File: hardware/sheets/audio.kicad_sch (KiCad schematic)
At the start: 17 parts, among them J1 PicoGUS_LineIn, J2 LineOut_TRS, U1 MCP6002

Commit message: JLCPCB sourcing pass: verify pinouts, LCSC part numbers, SMD build
Custom-symbol verification (open-questions Q5 resolved):
- MAX3241 symbol was wrong on nearly every pin and used MAX3243-style
  control names; regenerated to the real SSOP-28 pinout (SHDN#/EN#/
  R1OUTB/R2OUTB) and com_port rewired -- EN# must be GROUNDED (the old
  ~FORCEON-high would have disabled the receivers on real silicon)
- DS12C887 symbol wrong on 4 pins (DS=17, RESET#=18, IRQ#=19, SQW=23)

Sourcing (every part checked against the JLC DB; ~45 line items):
- New tools/parts.py maps (lib_id, value) -> LCSC; build.py applies it as
  an 'LCSC Part Num' property on every component (384 across the project)
- Sheets stay generic; stock-forced substitutions bound in the map:
  '374->'574 (parallel rewired), '163->'161, '157->HC157 (+HCT-buffered
  3.3V selects, I0/I1 swapped), '02->HC02, TCM809->MCP809, 2N3904->MMBT3904
- bus_mcu address counters moved to the 3.3V domain (HC161 on 3V3_BUS,
  loaded from MCU-side MD0-7; HCT244s read the 3.3V outputs at TTL Vih)
- 14.318 XOs are 3.3V-only parts: powered from 3V3, squared up via spare
  HCT gates (cpu_core U13, card_isatest U19)
- COM baud reference is now a 1.8432MHz crystal on the 16C550's XIN/XOUT
  (3.3V-only oscillators vs a 5V-only soft card)
- Supervisor QSPI header replaced with a real W25Q128JVSIQ
- Socket policy (fab installs sockets): V20 DIP-40, SRAM DIP-32 (no 5V
  512Kx8 SRAM at JLC at all), DS12C887 DIP-24, female headers for modules

Docs: CLAUDE.md fabrication-constraints section (SMD, 100x100mm, generic-
symbols rule, voltage-domain rule); README + hardware/README fab notes;
notes/jlcpcb-sourcing.md (decisions, thin-stock flags, not-at-JLC list);
stale questions-sidecar.md collapsed to its supersession record.

Rebuilt motherboard + cards: structural ERC 0, byte-identical rebuilds.

Co-Authored-By: Claude Fable 5 <noreply@anthropic.com>
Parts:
- C1, C7: LCSC Part Num (none) -> C15850
- C2: LCSC Part Num (none) -> C57112
- C3, C4, C5: LCSC Part Num (none) -> C15849
- C6: LCSC Part Num (none) -> C14663
- J1, J2: LCSC Part Num (none) -> C2337
- R1, R10, R2, R4, R5, R6: LCSC Part Num (none) -> C25804
- R3: LCSC Part Num (none) -> C21190
- U1: LCSC Part Num (none) -> C7377
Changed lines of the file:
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@@
+			)
+		)
+		(property "LCSC Part Num" "C25804"
+			(at 50.8 76.2 0)
+			(effects
+				(font
+					(size 1.27 1.27)
+				)
+				(hide yes)
 			)
 		)
@@
 			)
 		)
+		(property "LCSC Part Num" "C25804"
+			(at 50.8 109.22 0)
+			(effects
+				(font
+					(size 1.27 1.27)
+				)
+				(hide yes)
+			)
+		)
 		(pin "1"
 		)
@@
 			)
 		)
+		(property "LCSC Part Num" "C15850"
+			(at 76.2 109.22 0)
+			(effects
+				(font
+					(size 1.27 1.27)
+				)
+				(hide yes)
+			)
+		)
 		(pin "1"
 		)
@@
 			)
 		)
+		(property "LCSC Part Num" "C21190"
+			(at 50.8 165.1 0)
+			(effects
+				(font
+					(size 1.27 1.27)
+				)
+				(hide yes)
+			)
+		)
 		(pin "1"
 		)
@@
 			)
 		)
+		(property "LCSC Part Num" "C57112"
+			(at 76.2 198.12 0)
+			(effects
+				(font
+					(size 1.27 1.27)
+				)
+				(hide yes)
+			)
+		)
 		(pin "1"
 		)
@@
 			)
 		)
+		(property "LCSC Part Num" "C15849"
+			(at 101.6 165.1 0)
+			(effects
+				(font
+					(size 1.27 1.27)
+				)
+				(hide yes)
+			)
+		)
 		(pin "1"
 		)
@@
 			)
 		)
+		(property "LCSC Part Num" "C2337"
+			(at 50.8 228.6 0)
+			(effects
+				(font
+					(size 1.27 1.27)
+				)
+				(hide yes)
+			)
+		)
 		(pin "1"
 		)
@@
 			)
 		)
+		(property "LCSC Part Num" "C15849"
+			(at 101.6 215.9 0)
+			(effects
+				(font
+					(size 1.27 1.27)
+				)
+				(hide yes)
+			)
+		)
 		(pin "1"
 		)
@@
 			)
 		)
+		(property "LCSC Part Num" "C15849"
+			(at 101.6 241.3 0)
+			(effects
+				(font
+					(size 1.27 1.27)
+				)
+				(hide yes)
+			)
+		)
 		(pin "1"
 		)
@@
 			)
 		)
+		(property "LCSC Part Num" "C7377"
+			(at 177.8 152.4 0)
+			(effects
+				(font
+					(size 1.27 1.27)
+				)
+				(hide yes)
+			)
+		)
 		(pin "3"
 		)
@@
 			)
 		)
+		(property "LCSC Part Num" "C14663"
+			(at 203.2 101.6 0)
+			(effects
+				(font
+					(size 1.27 1.27)
+				)
+				(hide yes)
+			)
+		)
 		(pin "1"
 		)
@@
 			)
 		)
+		(property "LCSC Part Num" "C25804"
+			(at 127 127 0)
+			(effects
+				(font
+					(size 1.27 1.27)
+				)
+				(hide yes)
+			)
+		)
 		(pin "1"
 		)
@@
 			)
 		)
+		(property "LCSC Part Num" "C25804"
+			(at 152.4 127 0)
+			(effects
+				(font
+					(size 1.27 1.27)
+				)
+				(hide yes)
+			)
+		)
 		(pin "1"
 		)
@@
 			)
 		)
+		(property "LCSC Part Num" "C25804"
+			(at 152.4 177.8 0)
+			(effects
+				(font
+					(size 1.27 1.27)
+				)
+				(hide yes)
+			)
+		)
 		(pin "1"
 		)
@@
 			)
 		)
+		(property "LCSC Part Num" "C25804"
+			(at 203.2 127 0)
+			(effects
+				(font
+					(size 1.27 1.27)
+				)
+				(hide yes)
+			)
+		)
 		(pin "1"
 		)
@@
 			)
 		)
+		(property "LCSC Part Num" "C15850"
+			(at 228.6 127 0)
+			(effects
+				(font
+					(size 1.27 1.27)
+				)
+				(hide yes)
+			)
+		)
 		(pin "1"
 		)
@@
 			(at 266.7 152.4 0)
 			(effects
+				(font
+					(size 1.27 1.27)
+				)
+				(hide yes)
+			)
+		)
+		(property "LCSC Part Num" "C2337"
+			(at 266.7 152.4 0)
+			(effects

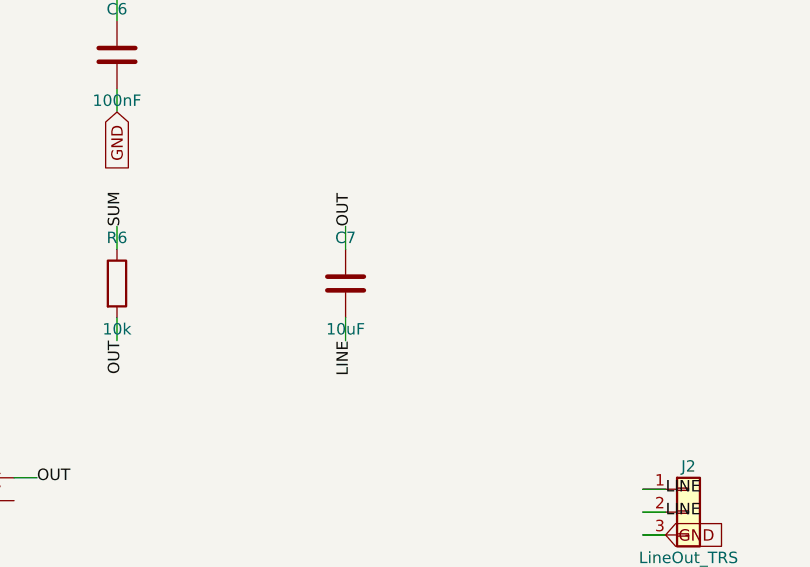
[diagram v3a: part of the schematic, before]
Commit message: Design review 2026-07-11: rail protection, decoupling, wiring fixes
Protection:
- Sidecar +5V now feeds through a 2A polyfuse into +5V_ISA with an
  SMBJ5.0A clamp + 22uF bulk (a faulted ISA card trips its own fuse
  instead of dropping the board; back-fed voltage is clamped).
- USB-C VBUS enters through a 3A polyfuse with an SMBJ5.0A on +5V
  (backstop for the CFG1 9-20V failure mode). CH224K gains a 1uF VDD
  cap; its PG routes to Supervisor GPIO16 as PD_PG. Buck output
  doubled to 2x22uF, 10uF at VIN, extra rail bulk.
- Supervisor USB-A host port: 27R series termination (RP2040
  requirement), USBLC6-2SC6 ESD array, 100uF VBUS bulk.
- Video: HDMI +5V fused (500mA), HPD sensed on GPIO41, 100R series on
  VGA sync. TMDS ESD array deferred to layout (no symbol).
- card_isatest: V5RAW bulk, Q1 gate soft-start cap, TVS on DUT rail.

Wiring fixes:
- SPKR had no driver anywhere (netlist: 1 node). Bus MCU GPIO22
  reassigned from the diagnostics-only bus-CLK sense to SPKR; bus_mcu
  drops CLK from its interface. Doc 5.2 updated.
- bus_mcu C8 decoupled +3V3, a rail that sheet never uses -> 3V3_BUS.
- Storage IRQ5 was push-pull (permanently driven when idle) -> 2N7002
  + gated '125 tri-state, same convention as the LPT IRQ7 stage.
- MAX3241 pump caps resized to the 5V datasheet values (47nF/330nF).
- LPT DB25 status inputs get 4.7k pull-ups (floated with no printer).
- Audio line-out gets a 100R series isolator before the jack.

Best practices:
- Decoupling to ~1x100nF per IC on every sheet + bulk per board
  (cpu_core 7->16 incl. the naked 3.3V oscillator, storage 4->11,
  parallel 6->13, rtc/com/video/bus_mcu/card_isatest similar).
- All floating spare CMOS inputs tied ('00/'74/'157/'02/'04/'125
  sections across cpu_core, bus_mcu, rtc, storage, card_isatest).

Sourcing: new parts mapped in parts.py with JLC-verified LCSC numbers;
Power_Protection lib registered in the tools; TPS563200 stock alert
(4 pcs left at JLC) flagged in parts.py + jlcpcb-sourcing.md. All
decisi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
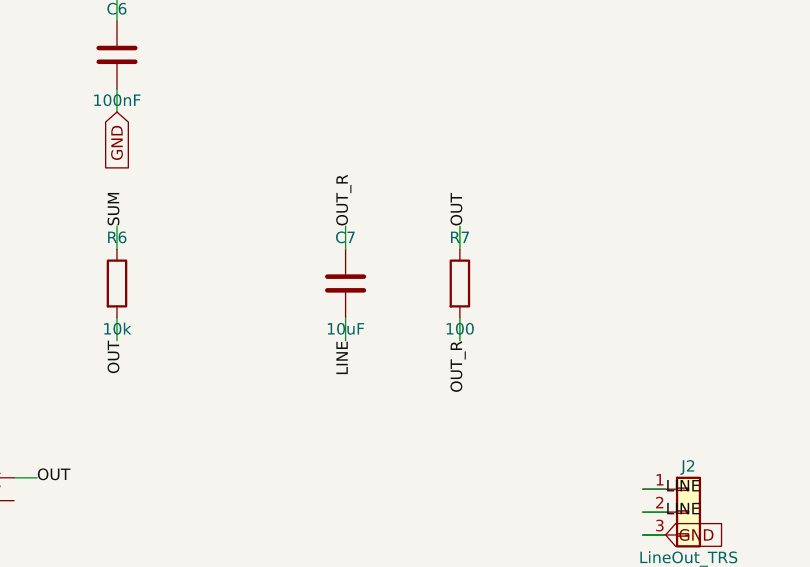
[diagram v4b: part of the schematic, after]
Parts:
- added J2: LineOut_TRS, symbol Connector_Generic:Conn_01x03
- C7: renamed from J2; value LineOut_TRS -> 10uF; symbol Connector_Generic:Conn_01x03 -> Device:C; LCSC Part Num C2337 -> C15850
- R7: renamed from C7; value 10uF -> 100; symbol Device:C -> Device:R; LCSC Part Num C15850 -> C22775
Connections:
- net GND: now also J2.3 (Pin_3); no longer C7.3 (Pin_3)
- net LINE: now also J2.1 (Pin_1), J2.2 (Pin_2); no longer C7.1 (Pin_1), R7.2
- new net OUT_R: C7.1, R7.2
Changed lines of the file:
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@@
+	(wire
+		(pts
+			(xy 241.3 123.19)
+			(xy 241.3 120.65)
+		)
+		(stroke
+			(width 0)
+			(type default)
+		)
+	)
+	(label "OUT"
+		(at 241.3 120.65 90)
+		(effects
+			(font
+				(size 1.27 1.27)
+			)
+		)
+	)
+	(wire
+		(pts
+			(xy 241.3 130.81)
+			(xy 241.3 133.35)
+		)
+		(stroke
+			(width 0)
+			(type default)
+		)
+	)
+	(label "OUT_R"
+		(at 241.3 133.35 270)
+		(effects
+			(font
+				(size 1.27 1.27)
+			)
+		)
+	)
 	(wire
 		(pts
@@
 		)
 	)
-	(label "OUT"
+	(label "OUT_R"
 		(at 228.6 120.65 90)
 		(effects
@@
 		(instances
 			(project "mini-xt"
-				(path "/26736c46-8b40-5460-874f-03596d17270c/130b8a0a-419b-58f7-be98-d1ab6f413e73"
+				(path "/26736c46-8b40-5460-874f-03596d17270c/eddc1827-22a2-582d-9105-2ac11ccaf77c"
 					(reference "R1101")
 					(unit 1)
@@
 		(instances
 			(project "mini-xt"
-				(path "/26736c46-8b40-5460-874f-03596d17270c/130b8a0a-419b-58f7-be98-d1ab6f413e73"
+				(path "/26736c46-8b40-5460-874f-03596d17270c/eddc1827-22a2-582d-9105-2ac11ccaf77c"
 					(reference "R1102")
 					(unit 1)
@@
 		(instances
 			(project "mini-xt"
-				(path "/26736c46-8b40-5460-874f-03596d17270c/130b8a0a-419b-58f7-be98-d1ab6f413e73"
+				(path "/26736c46-8b40-5460-874f-03596d17270c/eddc1827-22a2-582d-9105-2ac11ccaf77c"
 					(reference "C1101")
 					(unit 1)
@@
 		(instances
 			(project "mini-xt"
-				(path "/26736c46-8b40-5460-874f-03596d17270c/130b8a0a-419b-58f7-be98-d1ab6f413e73"
+				(path "/26736c46-8b40-5460-874f-03596d17270c/eddc1827-22a2-582d-9105-2ac11ccaf77c"
 					(reference "R1103")
 					(unit 1)
@@
 		(instances
 			(project "mini-xt"
-				(path "/26736c46-8b40-5460-874f-03596d17270c/130b8a0a-419b-58f7-be98-d1ab6f413e73"
+				(path "/26736c46-8b40-5460-874f-03596d17270c/eddc1827-22a2-582d-9105-2ac11ccaf77c"
 					(reference "C1102")
 					(unit 1)
@@
 		(instances
 			(project "mini-xt"
-				(path "/26736c46-8b40-5460-874f-03596d17270c/130b8a0a-419b-58f7-be98-d1ab6f413e73"
+				(path "/26736c46-8b40-5460-874f-03596d17270c/eddc1827-22a2-582d-9105-2ac11ccaf77c"
 					(reference "C1103")
 					(unit 1)
@@
 		(instances
 			(project "mini-xt"
-				(path "/26736c46-8b40-5460-874f-03596d17270c/130b8a0a-419b-58f7-be98-d1ab6f413e73"
+				(path "/26736c46-8b40-5460-874f-03596d17270c/eddc1827-22a2-582d-9105-2ac11ccaf77c"
 					(reference "J1101")
 					(unit 1)
@@
 		(instances
 			(project "mini-xt"
-				(path "/26736c46-8b40-5460-874f-03596d17270c/130b8a0a-419b-58f7-be98-d1ab6f413e73"
+				(path "/26736c46-8b40-5460-874f-03596d17270c/eddc1827-22a2-582d-9105-2ac11ccaf77c"
 					(reference "C1104")
 					(unit 1)
@@
 		(instances
 			(project "mini-xt"
-				(path "/26736c46-8b40-5460-874f-03596d17270c/130b8a0a-419b-58f7-be98-d1ab6f413e73"
+				(path "/26736c46-8b40-5460-874f-03596d17270c/eddc1827-22a2-582d-9105-2ac11ccaf77c"
 					(reference "C1105")
 					(unit 1)
@@
 		(instances
 			(project "mini-xt"
-				(path "/26736c46-8b40-5460-874f-03596d17270c/130b8a0a-419b-58f7-be98-d1ab6f413e73"
+				(path "/26736c46-8b40-5460-874f-03596d17270c/eddc1827-22a2-582d-9105-2ac11ccaf77c"
 					(reference "U1101")
 					(unit 1)
@@
 		(instances
 			(project "mini-xt"
-				(path "/26736c46-8b40-5460-874f-03596d17270c/130b8a0a-419b-58f7-be98-d1ab6f413e73"
+				(path "/26736c46-8b40-5460-874f-03596d17270c/eddc1827-22a2-582d-9105-2ac11ccaf77c"
 					(reference "C1106")
 					(unit 1)
@@
 		(instances
 			(project "mini-xt"
-				(path "/26736c46-8b40-5460-874f-03596d17270c/130b8a0a-419b-58f7-be98-d1ab6f413e73"
+				(path "/26736c46-8b40-5460-874f-03596d17270c/eddc1827-22a2-582d-9105-2ac11ccaf77c"
 					(reference "R1104")
 					(unit 1)
@@
 		(instances
 			(project "mini-xt"
-				(path "/26736c46-8b40-5460-874f-03596d17270c/130b8a0a-419b-58f7-be98-d1ab6f413e73"
+				(path "/26736c46-8b40-5460-874f-03596d17270c/eddc1827-22a2-582d-9105-2ac11ccaf77c"
 					(reference "R1105")
 					(unit 1)
@@
 		(instances
 			(project "mini-xt"
-				(path "/26736c46-8b40-5460-874f-03596d17270c/130b8a0a-419b-58f7-be98-d1ab6f413e73"
+				(path "/26736c46-8b40-5460-874f-03596d17270c/eddc1827-22a2-582d-9105-2ac11ccaf77c"
 					(reference "R1110")
 					(unit 1)
@@
 		(instances
 			(project "mini-xt"
-				(path "/26736c46-8b40-5460-874f-03596d17270c/130b8a0a-419b-58f7-be98-d1ab6f413e73"
+				(path "/26736c46-8b40-5460-874f-03596d17270c/eddc1827-22a2-582d-9105-2ac11ccaf77c"
 					(reference "R1106")
+					(unit 1)
+				)
+			)
+		)
+	)
+	(symbol
+		(lib_id "Device:R")
+		(at 241.3 127 0)
+		(unit 1)
+		(exclude_from_sim no)
+		(in_bom yes)
+		(on_board yes)
+		(dnp no)
+		(fields_autoplaced yes)
+		(property "Reference" "R7"
+			(at 241.3 121.92 0)
+			(effects
+				(font
+					(size 1.27 1.27)
+				)
+			)
+		)
+		(property "Value" "100"
+			(at 241.3 132.08 0)
+			(effects
+				(font
+					(size 1.27 1.27)
+				)
+			)
+		)
+		(property "Footprint" ""
+			(at 241.3 127 0)
+			(effects
+				(font
+					(size 1.27 1.27)
+				)
+				(hide yes)
+			)
+		)
+		(property "LCSC Part Num" "C22775"
+			(at 241.3 127 0)
+			(effects
+				(font
+					(size 1.27 1.27)
+				)
+				(hide yes)
+			)
+		)
+		(pin "1"
+		)
+		(pin "2"
+		)
+		(instances
+			(project "mini-xt"
+				(path "/26736c46-8b40-5460-874f-03596d17270c/eddc1827-22a2-582d-9105-2ac11ccaf77c"
+					(reference "R1107")
 					(unit 1)
 				)
@@
 		(instances
 			(project "mini-xt"
-				(path "/26736c46-8b40-5460-874f-03596d17270c/130b8a0a-419b-58f7-be98-d1ab6f413e73"
+				(path "/26736c46-8b40-5460-874f-03596d17270c/eddc1827-22a2-582d-9105-2ac11ccaf77c"
 					(reference "C1107")
 					(unit 1)
@@
 		(instances
 			(project "mini-xt"
-				(path "/26736c46-8b40-5460-874f-03596d17270c/130b8a0a-419b-58f7-be98-d1ab6f413e73"
+				(path "/26736c46-8b40-5460-874f-03596d17270c/eddc1827-22a2-582d-9105-2ac11ccaf77c"
 					(reference "J1102")
 					(unit 1)
